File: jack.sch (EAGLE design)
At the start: 29 parts, among them IC1 NUF2221W1T2G, IC2 ATSAMD21G18, IC3 LDO, SW1 SPST, X1 TSX-3225 24.0000MF10Z-C3

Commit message: Minor changes
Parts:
- added JP3: SAM_ARM_JTAG, jack:SAM_ARM_JTAG
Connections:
- new net N$1: JP3.VCC
- new net N$10: JP3.TCK
- new net N$11: JP3.TMS
- new net N$2: JP3.GND@1
- new net N$4: JP3.GND@2
- new net N$5: JP3.(KEY)
- new net N$6: JP3.GND@3
- new net N$7: JP3.NRESET
- new net N$8: JP3.TDI
- new net N$9: JP3.TDO
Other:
- note added: "JTAG Header"
- moved on the sheet: C12, C13, X1
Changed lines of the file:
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@@
 <part name="LOGO1" library="SparkFun-Aesthetics" deviceset="OSHW-LOGO" device="L"/>
 <part name="JP2" library="pinhead" deviceset="PINHD-1X22" device=""/>
+<part name="JP3" library="jack" deviceset="SAM_ARM_JTAG" device=""/>
 </parts>
 <sheets>
@@
 <wire x1="146.05" y1="16.51" x2="147.32" y2="-54.61" width="0.1524" layer="97" style="longdash"/>
 <wire x1="147.32" y1="-54.61" x2="147.32" y2="-105.41" width="0.1524" layer="97" style="longdash"/>
-<wire x1="147.32" y1="-105.41" x2="102.87" y2="-105.41" width="0.1524" layer="97" style="longdash"/>
-<wire x1="102.87" y1="-105.41" x2="64.77" y2="-105.41" width="0.1524" layer="97" style="longdash"/>
+<wire x1="147.32" y1="-105.41" x2="101.6" y2="-105.41" width="0.1524" layer="97" style="longdash"/>
+<wire x1="101.6" y1="-105.41" x2="64.77" y2="-105.41" width="0.1524" layer="97" style="longdash"/>
 <wire x1="64.77" y1="-105.41" x2="34.29" y2="-105.41" width="0.1524" layer="97" style="longdash"/>
 <wire x1="34.29" y1="-105.41" x2="-41.91" y2="-105.41" width="0.1524" layer="97" style="longdash"/>
@@
 <text x="-17.78" y="-58.42" size="1.778" layer="97">Digital power and filter</text>
 <text x="39.37" y="-58.42" size="1.778" layer="97">Reset pushbutton</text>
-<text x="74.93" y="-58.42" size="1.778" layer="97">External clock</text>
+<text x="76.2" y="-58.42" size="1.778" layer="97">External clock</text>
 <text x="111.76" y="12.7" size="1.778" layer="97">ATSAMD21 Breakout</text>
 <wire x1="-105.41" y1="-74.93" x2="-105.41" y2="-31.75" width="0.1524" layer="97" style="longdash"/>
@@
 <wire x1="-41.91" y1="-54.61" x2="34.29" y2="-54.61" width="0.1524" layer="97" style="shortdash"/>
 <wire x1="34.29" y1="-54.61" x2="64.77" y2="-54.61" width="0.1524" layer="97" style="shortdash"/>
-<wire x1="64.77" y1="-54.61" x2="102.87" y2="-54.61" width="0.1524" layer="97" style="shortdash"/>
-<wire x1="102.87" y1="-54.61" x2="147.32" y2="-54.61" width="0.1524" layer="97" style="shortdash"/>
+<wire x1="64.77" y1="-54.61" x2="101.6" y2="-54.61" width="0.1524" layer="97" style="shortdash"/>
+<wire x1="101.6" y1="-54.61" x2="147.32" y2="-54.61" width="0.1524" layer="97" style="shortdash"/>
 <wire x1="34.29" y1="-54.61" x2="34.29" y2="-105.41" width="0.1524" layer="97" style="shortdash"/>
-<wire x1="64.77" y1="-54.61" x2="64.77" y2="-105.41" width="0.1524" layer="97" style="shortdash"/>
-<wire x1="102.87" y1="-54.61" x2="102.87" y2="-105.41" width="0.1524" layer="97" style="shortdash"/>
+<wire x1="64.77" y1="-54.61" x2="64.77" y2="-81.28" width="0.1524" layer="97" style="shortdash"/>
+<wire x1="64.77" y1="-81.28" x2="64.77" y2="-105.41" width="0.1524" layer="97" style="shortdash"/>
+<wire x1="101.6" y1="-54.61" x2="101.6" y2="-81.28" width="0.1524" layer="97" style="shortdash"/>
 <text x="104.14" y="-102.87" size="1.778" layer="97">Created by Michele Perla
 2015
 https://hackaday.io/project/6062-jack</text>
 <text x="104.14" y="-58.42" size="1.778" layer="97">JACK - Just Another Cortex Kit</text>
+<text x="76.2" y="-85.09" size="1.778" layer="95">JTAG Header</text>
+<wire x1="101.6" y1="-81.28" x2="101.6" y2="-105.41" width="0.1524" layer="97" style="shortdash"/>
+<wire x1="64.77" y1="-81.28" x2="101.6" y2="-81.28" width="0.1524" layer="97" style="shortdash"/>
 </plain>
 <instances>
@@
 <instance part="C10" gate="G$1" x="-90.17" y="-57.15" rot="MR0"/>
 <instance part="C11" gate="G$1" x="-57.15" y="-57.15"/>
-<instance part="X1" gate="G$1" x="82.55" y="-80.01"/>
-<instance part="C12" gate="G$1" x="73.66" y="-83.82" rot="MR0"/>
-<instance part="C13" gate="G$1" x="91.44" y="-83.82"/>
-<instance part="GND9" gate="G$1" x="82.55" y="-90.17"/>
+<instance part="X1" gate="G$1" x="82.55" y="-64.77"/>
+<instance part="C12" gate="G$1" x="73.66" y="-68.58" rot="MR0"/>
+<instance part="C13" gate="G$1" x="91.44" y="-68.58"/>
+<instance part="GND9" gate="G$1" x="82.55" y="-74.93"/>
 <instance part="D1" gate="G$1" x="-90.17" y="-46.99" rot="R270"/>
 <instance part="D2" gate="G$1" x="-97.79" y="-46.99" rot="R270"/>
@@
 <instance part="LOGO1" gate="G$1" x="124.46" y="-74.93"/>
 <instance part="JP2" gate="A" x="129.54" y="-20.32" rot="R180"/>
+<instance part="JP3" gate="G$1" x="82.55" y="-91.44"/>
 </instances>
 <busses>
@@
 <segment>
 <pinref part="C12" gate="G$1" pin="2"/>
-<wire x1="73.66" y1="-88.9" x2="73.66" y2="-90.17" width="0.1524" layer="91"/>
-<wire x1="73.66" y1="-90.17" x2="80.01" y2="-90.17" width="0.1524" layer="91"/>
+<wire x1="73.66" y1="-73.66" x2="73.66" y2="-74.93" width="0.1524" layer="91"/>
+<wire x1="73.66" y1="-74.93" x2="80.01" y2="-74.93" width="0.1524" layer="91"/>
 <pinref part="C13" gate="G$1" pin="2"/>
-<wire x1="80.01" y1="-90.17" x2="82.55" y2="-90.17" width="0.1524" layer="91"/>
-<wire x1="82.55" y1="-90.17" x2="85.09" y2="-90.17" width="0.1524" layer="91"/>
-<wire x1="85.09" y1="-90.17" x2="91.44" y2="-90.17" width="0.1524" layer="91"/>
-<wire x1="91.44" y1="-90.17" x2="91.44" y2="-88.9" width="0.1524" layer="91"/>
+<wire x1="80.01" y1="-74.93" x2="82.55" y2="-74.93" width="0.1524" layer="91"/>
+<wire x1="82.55" y1="-74.93" x2="85.09" y2="-74.93" width="0.1524" layer="91"/>
+<wire x1="85.09" y1="-74.93" x2="91.44" y2="-74.93" width="0.1524" layer="91"/>
+<wire x1="91.44" y1="-74.93" x2="91.44" y2="-73.66" width="0.1524" layer="91"/>
 <pinref part="X1" gate="G$1" pin="GND@1"/>
-<wire x1="80.01" y1="-85.09" x2="80.01" y2="-90.17" width="0.1524" layer="91"/>
+<wire x1="80.01" y1="-69.85" x2="80.01" y2="-74.93" width="0.1524" layer="91"/>
 <pinref part="X1" gate="G$1" pin="GND@2"/>
-<wire x1="85.09" y1="-85.09" x2="85.09" y2="-90.17" width="0.1524" layer="91"/>
-<junction x="80.01" y="-90.17"/>
-<junction x="85.09" y="-90.17"/>
-<junction x="82.55" y="-90.17"/>
+<wire x1="85.09" y1="-69.85" x2="85.09" y2="-74.93" width="0.1524" layer="91"/>
+<junction x="80.01" y="-74.93"/>
+<junction x="85.09" y="-74.93"/>
+<junction x="82.55" y="-74.93"/>
 <pinref part="GND9" gate="G$1" pin="GND"/>
 </segment>
@@
 <segment>
 <pinref part="X1" gate="G$1" pin="P$1"/>
-<wire x1="74.93" y1="-80.01" x2="73.66" y2="-80.01" width="0.1524" layer="91"/>
+<wire x1="74.93" y1="-64.77" x2="73.66" y2="-64.77" width="0.1524" layer="91"/>
 <pinref part="C12" gate="G$1" pin="1"/>
-<wire x1="73.66" y1="-80.01" x2="73.66" y2="-81.28" width="0.1524" layer="91"/>
-<junction x="73.66" y="-80.01"/>
-<wire x1="73.66" y1="-80.01" x2="72.39" y2="-80.01" width="0.1524" layer="91"/>
-<label x="72.39" y="-80.01" size="1.27" layer="95" rot="R180" xref="yes"/>
+<wire x1="73.66" y1="-64.77" x2="73.66" y2="-66.04" width="0.1524" layer="91"/>
+<junction x="73.66" y="-64.77"/>
+<wire x1="73.66" y1="-64.77" x2="72.39" y2="-64.77" width="0.1524" layer="91"/>
+<label x="72.39" y="-64.77" size="1.27" layer="95" rot="R180" xref="yes"/>
 </segment>
 </net>
@@
 <segment>
 <pinref part="X1" gate="G$1" pin="P$3"/>
-<wire x1="90.17" y1="-80.01" x2="91.44" y2="-80.01" width="0.1524" layer="91"/>
+<wire x1="90.17" y1="-64.77" x2="91.44" y2="-64.77" width="0.1524" layer="91"/>
 <pinref part="C13" gate="G$1" pin="1"/>
-<wire x1="91.44" y1="-80.01" x2="91.44" y2="-81.28" width="0.1524" layer="91"/>
-<junction x="91.44" y="-80.01"/>
-<wire x1="91.44" y1="-80.01" x2="92.71" y2="-80.01" width="0.1524" layer="91"/>
-<label x="92.71" y="-80.01" size="1.27" layer="95" xref="yes"/>
+<wire x1="91.44" y1="-64.77" x2="91.44" y2="-66.04" width="0.1524" layer="91"/>
+<junction x="91.44" y="-64.77"/>
+<wire x1="91.44" y1="-64.77" x2="92.71" y2="-64.77" width="0.1524" layer="91"/>
+<label x="92.71" y="-64.77" size="1.27" layer="95" xref="yes"/>
 </segment>
 </net>
@@
 </segment>
 </net>
+<net name="N$1" class="0">
+<segment>
+<pinref part="JP3" gate="G$1" pin="VCC"/>
+<wire x1="69.85" y1="-91.44" x2="68.58" y2="-91.44" width="0.1524" layer="91"/>
+</segment>
+</net>
+<net name="N$2" class="0">
+<segment>
+<pinref part="JP3" gate="G$1" pin="GND@1"/>
+<wire x1="69.85" y1="-93.98" x2="68.58" y2="-93.98" width="0.1524" layer="91"/>
+</segment>
+</net>
+<net name="N$4" class="0">
+<segment>
+<pinref part="JP3" gate="G$1" pin="GND@2"/>
+<wire x1="69.85" y1="-96.52" x2="68.58" y2="-96.52" width="0.1524" layer="91"/>
+</segment>
+</net>
+<net name="N$5" class="0">
+<segment>
+<pinref part="JP3" gate="G$1" pin="(KEY)"/>
+<wire x1="69.85" y1="-99.06" x2="68.58" y2="-99.06" width="0.1524" layer="91"/>
+</segment>
+</net>
+<net name="N$6" class="0">
+<segment>
+<pinref part="JP3" gate="G$1" pin="GND@3"/>
+<wire x1="69.85" y1="-101.6" x2="68.58" y2="-101.6" width="0.1524" layer="91"/>
+</segment>
+</net>
+<net name="N$7" class="0">
+<segment>
+<pinref part="JP3" gate="G$1" pin="NRESET"/>
+<wire x1="95.25" y1="-101.6" x2="96.52" y2="-101.6" width="0.1524" layer="91"/>
+</segment>
+</net>
+<net name="N$8" class="0">
+<segment>
+<pinref part="JP3" gate="G$1" pin="TDI"/>
+<wire x1="95.25" y1="-99.06" x2="96.52" y2="-99.06" width="0.1524" layer="91"/>
+</segment>
+</net>
+<net name="N$9" class="0">
+<segment>
+<pinref part="JP3" gate="G$1" pin="TDO"/>
+<wire x1="95.25" y1="-96.52" x2="96.52" y2="-96.52" width="0.1524" layer="91"/>
+</segment>
+</net>
+<net name="N$10" class="0">
+<segment>
+<pinref part="JP3" gate="G$1" pin="TCK"/>
+<wire x1="95.25" y1="-93.98" x2="96.52" y2="-93.98" width="0.1524" layer="91"/>
+</segment>
+</net>
+<net name="N$11" class="0">
+<segment>
+<pinref part="JP3" gate="G$1" pin="TMS"/>
+<wire x1="95.25" y1="-91.44" x2="96.52" y2="-91.44" width="0.1524" layer="91"/>
+</segment>
+</net>

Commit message: :satellite: Modified .gitignore, updated schematic, progressing layout
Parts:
- removed JP3: SAM_ARM_JTAG, jack:SAM_ARM_JTAG
- added R4: 0, rcl:R-EU_R0603
- C1, C10, C12, C13, C2, C3, C4, C5, C9: device rcl:C-EUC0603 -> rcl:C-EUC0402K
- SW1: value SPST -> SPST3.5X6MM; device jack:SPST -> jack:SPST3.5X6MM
- X1: device jack:XTAL -> jack:XTALCX-3225
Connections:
- net 45 renamed SWCLK
- net 46 renamed SWDIO
- removed net N$1: JP3.VCC
- removed net N$10: JP3.TCK
- removed net N$11: JP3.TMS
- removed net N$2: JP3.GND@1
- removed net N$4: JP3.GND@2
- removed net N$5: JP3.(KEY)
- removed net N$6: JP3.GND@3
- removed net N$7: JP3.NRESET
- removed net N$8: JP3.TDI
- removed net N$9: JP3.TDO
- net GND: now also R4.1
- net GNDANA: now also R4.2
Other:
- note removed: "JTAG Header"
- moved on the sheet: C12, C13, X1

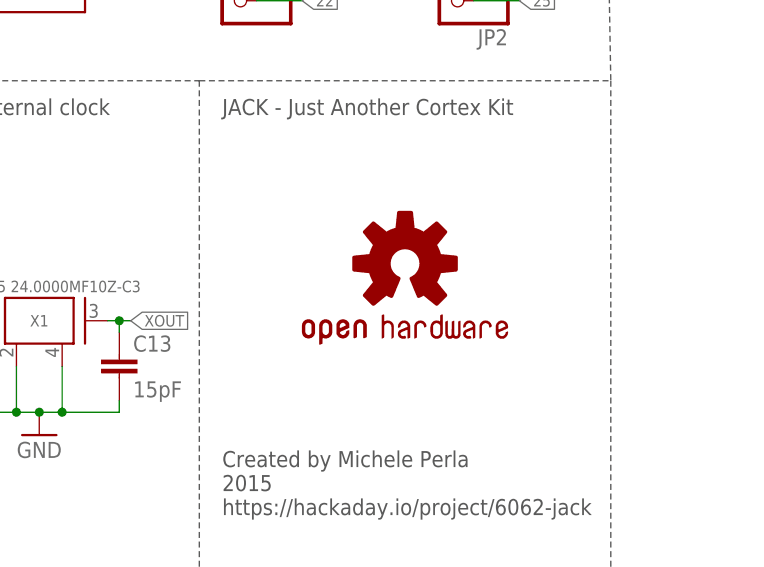
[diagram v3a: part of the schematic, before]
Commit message: Started power signals layout
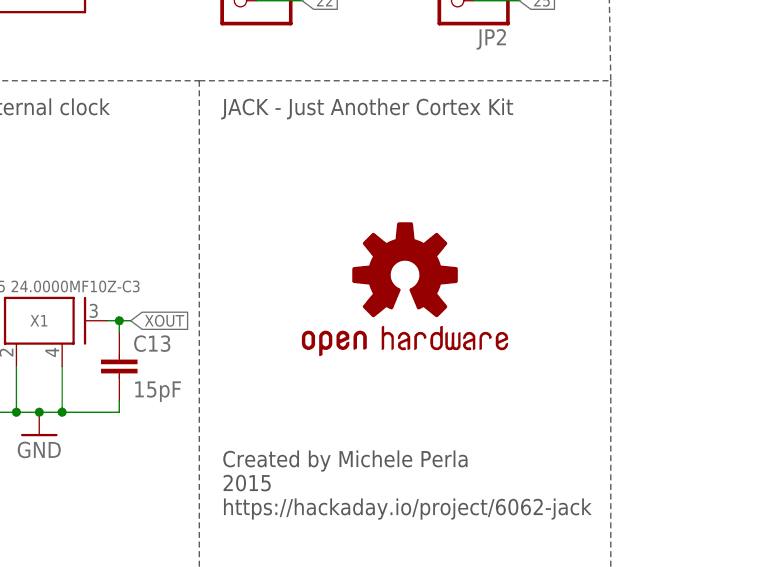
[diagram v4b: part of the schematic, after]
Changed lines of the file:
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@@
 <instance part="JP1" gate="A" x="105.41" y="-17.78" rot="MR0"/>
 <instance part="VDD5" gate="G$1" x="-36.83" y="-64.77"/>
-<instance part="LOGO1" gate="G$1" x="124.46" y="-74.93"/>
+<instance part="LOGO1" gate="G$1" x="124.46" y="-76.2"/>
 <instance part="JP2" gate="A" x="129.54" y="-20.32" rot="R180"/>
 <instance part="R4" gate="G$1" x="-52.07" y="-101.6" rot="R180"/>

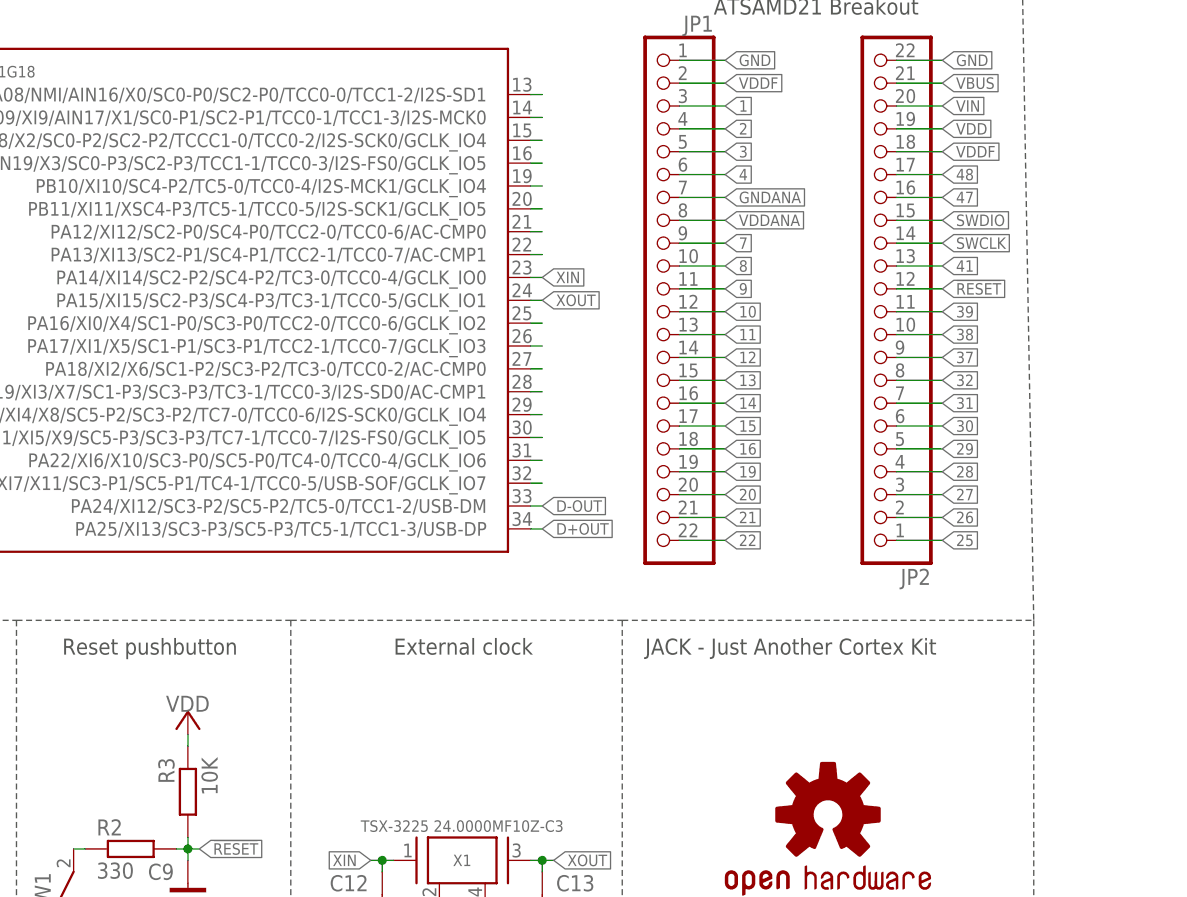
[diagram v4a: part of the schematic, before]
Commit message: :thumbsup: Updated mcu pins/breakout header map
I'm mapping the pins of the ATSAM21D to the breakout header in a way
that reduces airwires length on the PCB, thus easing the layout process
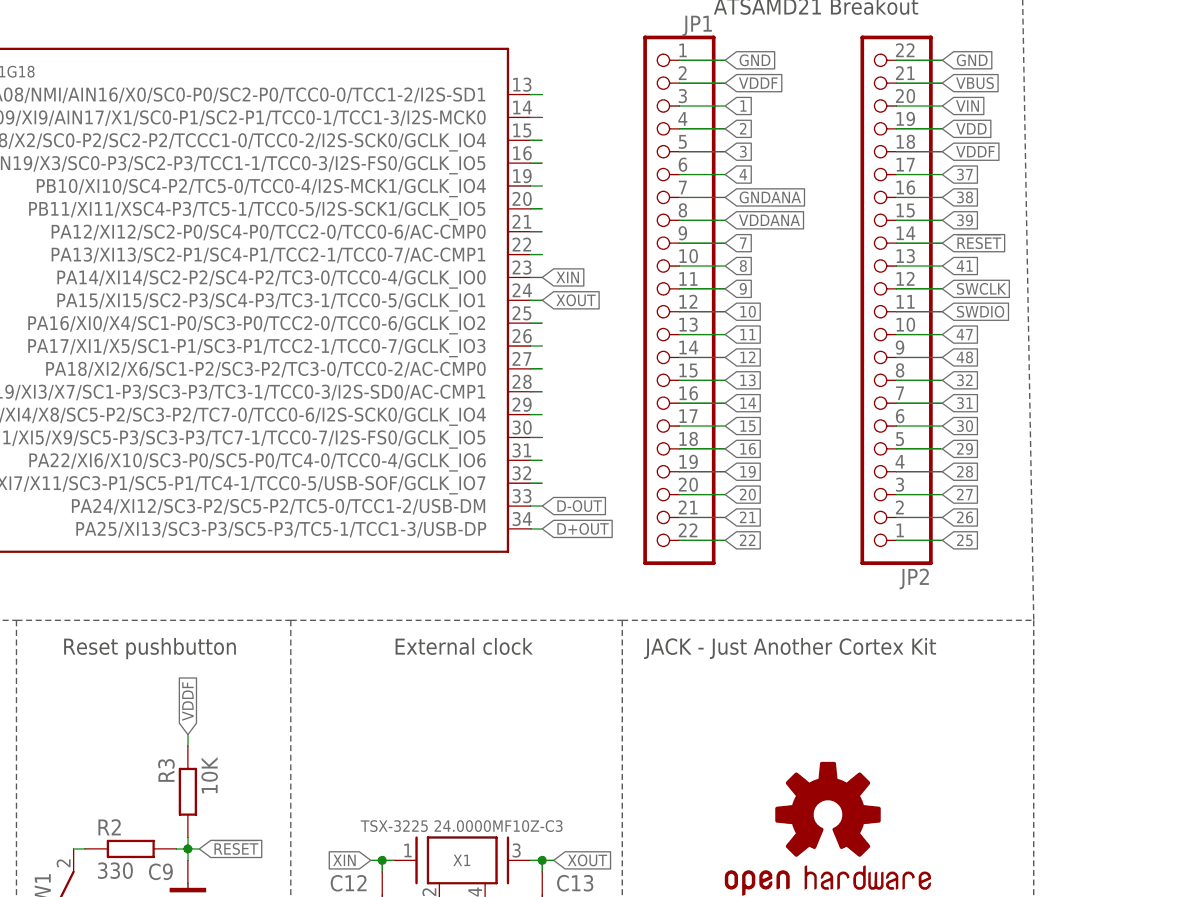
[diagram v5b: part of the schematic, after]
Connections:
- net !RESET: now also JP2.14; no longer JP2.12
- net 37: now also JP2.17; no longer JP2.9
- net 38: now also JP2.16; no longer JP2.10
- net 39: now also JP2.15; no longer JP2.11
- net 47: now also JP2.10; no longer JP2.16
- net 48: now also JP2.9; no longer JP2.17
- net SWCLK: now also JP2.12; no longer JP2.14
- net SWDIO: now also JP2.11; no longer JP2.15
- net VDD: no longer R3.1
- net VDDF: now also R3.1

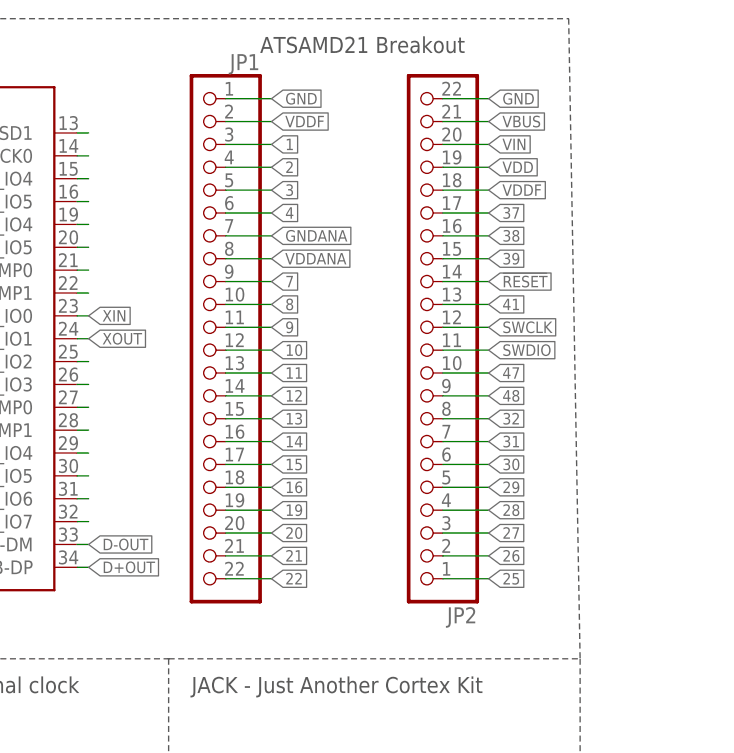
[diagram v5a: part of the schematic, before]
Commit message: PCB layout almost done, changed breakout configuration accordingly
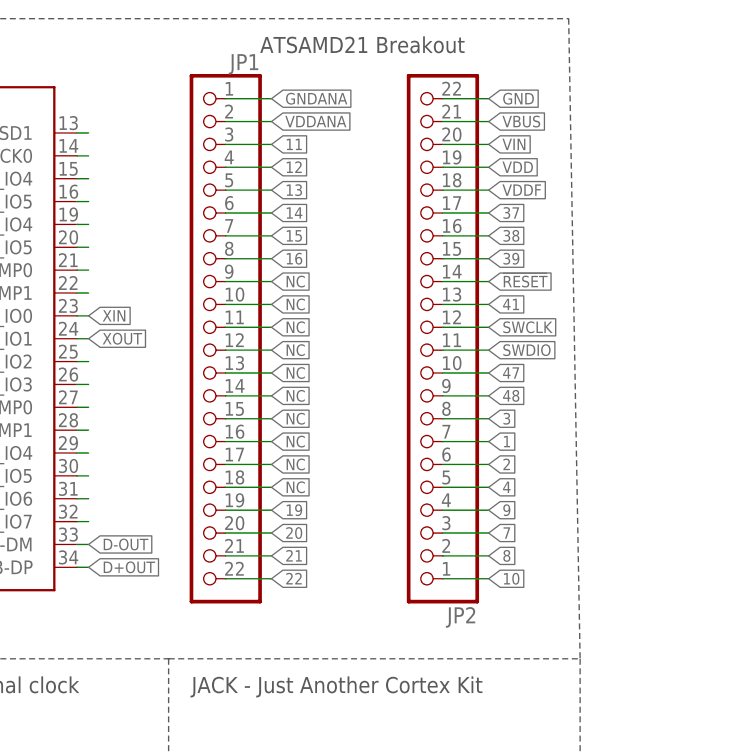
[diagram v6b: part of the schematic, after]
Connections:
- new net NC: JP1.10, JP1.11, JP1.12, JP1.13, JP1.14, JP1.15, JP1.16, JP1.17, JP1.18, JP1.9
- net 1: now also JP2.7; no longer JP1.3
- net 10: now also JP2.1; no longer JP1.12
- net 11: now also JP1.3; no longer JP1.13
- net 12: now also JP1.4; no longer JP1.14
- net 13: now also JP1.5; no longer JP1.15
- net 14: now also JP1.6; no longer JP1.16
- net 15: now also JP1.7; no longer JP1.17
- net 16: now also JP1.8; no longer JP1.18
- net 2: now also JP2.6; no longer JP1.4
- net 25: no longer JP2.1
- net 26: no longer JP2.2
- net 27: no longer JP2.3
- net 28: no longer JP2.4
- net 29: no longer JP2.5
- net 3: now also JP2.8; no longer JP1.5
- net 30: no longer JP2.6
- net 31: no longer JP2.7
- net 32: no longer JP2.8
- net 4: now also JP2.5; no longer JP1.6
- net 7: now also JP2.3; no longer JP1.9
- net 8: now also JP2.2; no longer JP1.10
- net 9: now also JP2.4; no longer JP1.11
- net GND: no longer JP1.1
- net GNDANA: now also JP1.1; no longer JP1.7
- net VDDANA: now also JP1.2; no longer JP1.8
- net VDDF: no longer JP1.2
